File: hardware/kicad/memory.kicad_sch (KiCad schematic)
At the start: 21 parts, among them J201 microSD, U201 IS42S16400J-6TLI, U202 W25Q128JVSIQ

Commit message: Main PCB placement, layout rules, clock terminations, offline freerouting
- place_main_pcb.py: hand floorplan for the ICs plus a greedy placer
  (parts next to what they connect to, decoupling at their IC's power
  pins, clock series resistors at their MCU pins), inner planes
  In1 = GND / In2 = +3V3. CAP1188 moved top-middle between J302/J303.
- Net classes (Power, Rail3V3, Touch, Clock) set by gen_main_pcb.py and
  exported to the router; stm32-epaper.kicad_dru adds length/skew limits
  for the SDRAM/SDIO/QSPI buses, USB pair, crystals and touch lines,
  checked by KiCad DRC after routing.
- Schematic: 22/33R source series resistors R208-R210 on the SDRAM,
  microSD and QSPI clocks; check_schematic.py verifies they bridge the
  right nets.
- route_main_pcb.py: Specctra DSN/SES round trip for headless freerouting.
- .mcp.json: freerouting MCP server switched to the local jar (offline, no
  API key).
- docs/DS_stm32f469ae.pdf added; LSE margin checked (needs high-drive mode).
- Enclosure: fit-check print export (chin section + knob) and checklist.

Co-Authored-By: Claude Opus 5.5 <noreply@anthropic.com>
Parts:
- added R208, R210: 22R, Resistor_SMD:R_0402_1005Metric, symbol Device:R
- added R209: 33R, Resistor_SMD:R_0402_1005Metric, symbol Device:R
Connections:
- net FMC_SDCLK: now also R208.1; no longer U201.38 (CLK)
- net QUADSPI_CLK: now also R210.1; no longer U202.6 (CLK)
- net SDIO_CK: now also R209.1; no longer J201.5 (CLK)
- new net QSPI_FLASH_CLK: R210.2, U202.6 (CLK)
- new net SDCARD_CLK: J201.5 (CLK), R209.2
- new net SDRAM_CLK: R208.2, U201.38 (CLK)
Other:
- note added: "Clock series resistors (22-33R), placed right at the MCU pin: source termination for the SDRAM, microSD and QSPI clocks (point-to-point, up to 90 MHz)."

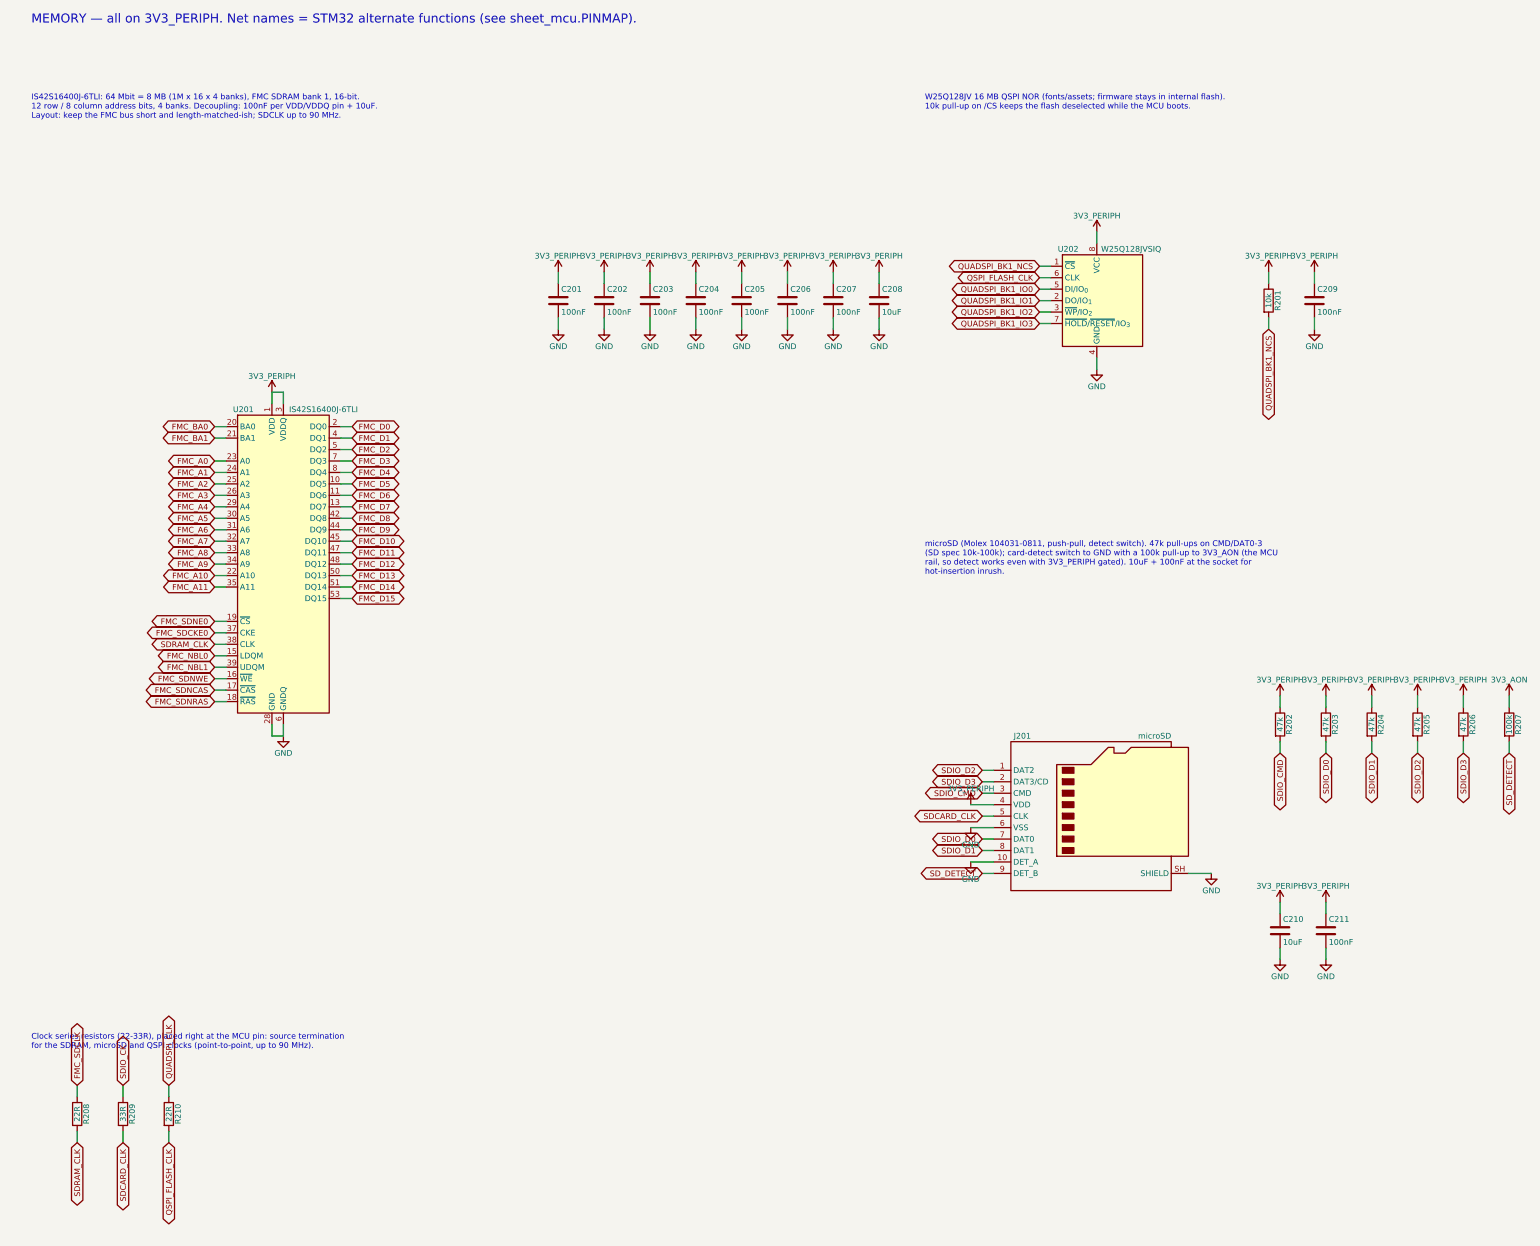
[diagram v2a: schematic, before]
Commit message: Schematic: Memory sheet redrawn with wired circuits
SDRAM VDD/VDDQ and QSPI VCC wired onto 3V3_PERIPH rails with their
decoupling banks; QSPI /CS pull-up tees off the line; microSD pull-ups
hang from a rail and drop onto each signal, VDD joins the rail with the
bulk/HF caps, VSS + DET_A share a GND column; the three clock series
resistors are drawn inline (device-side net names kept by label).
conn_by_name gains drawn= for pins the caller wires itself.
compare_netlists: electrically identical; board re-synced (0 unconnected,
0 parity issues).

Co-Authored-By: Claude Opus 5.5 <noreply@anthropic.com>
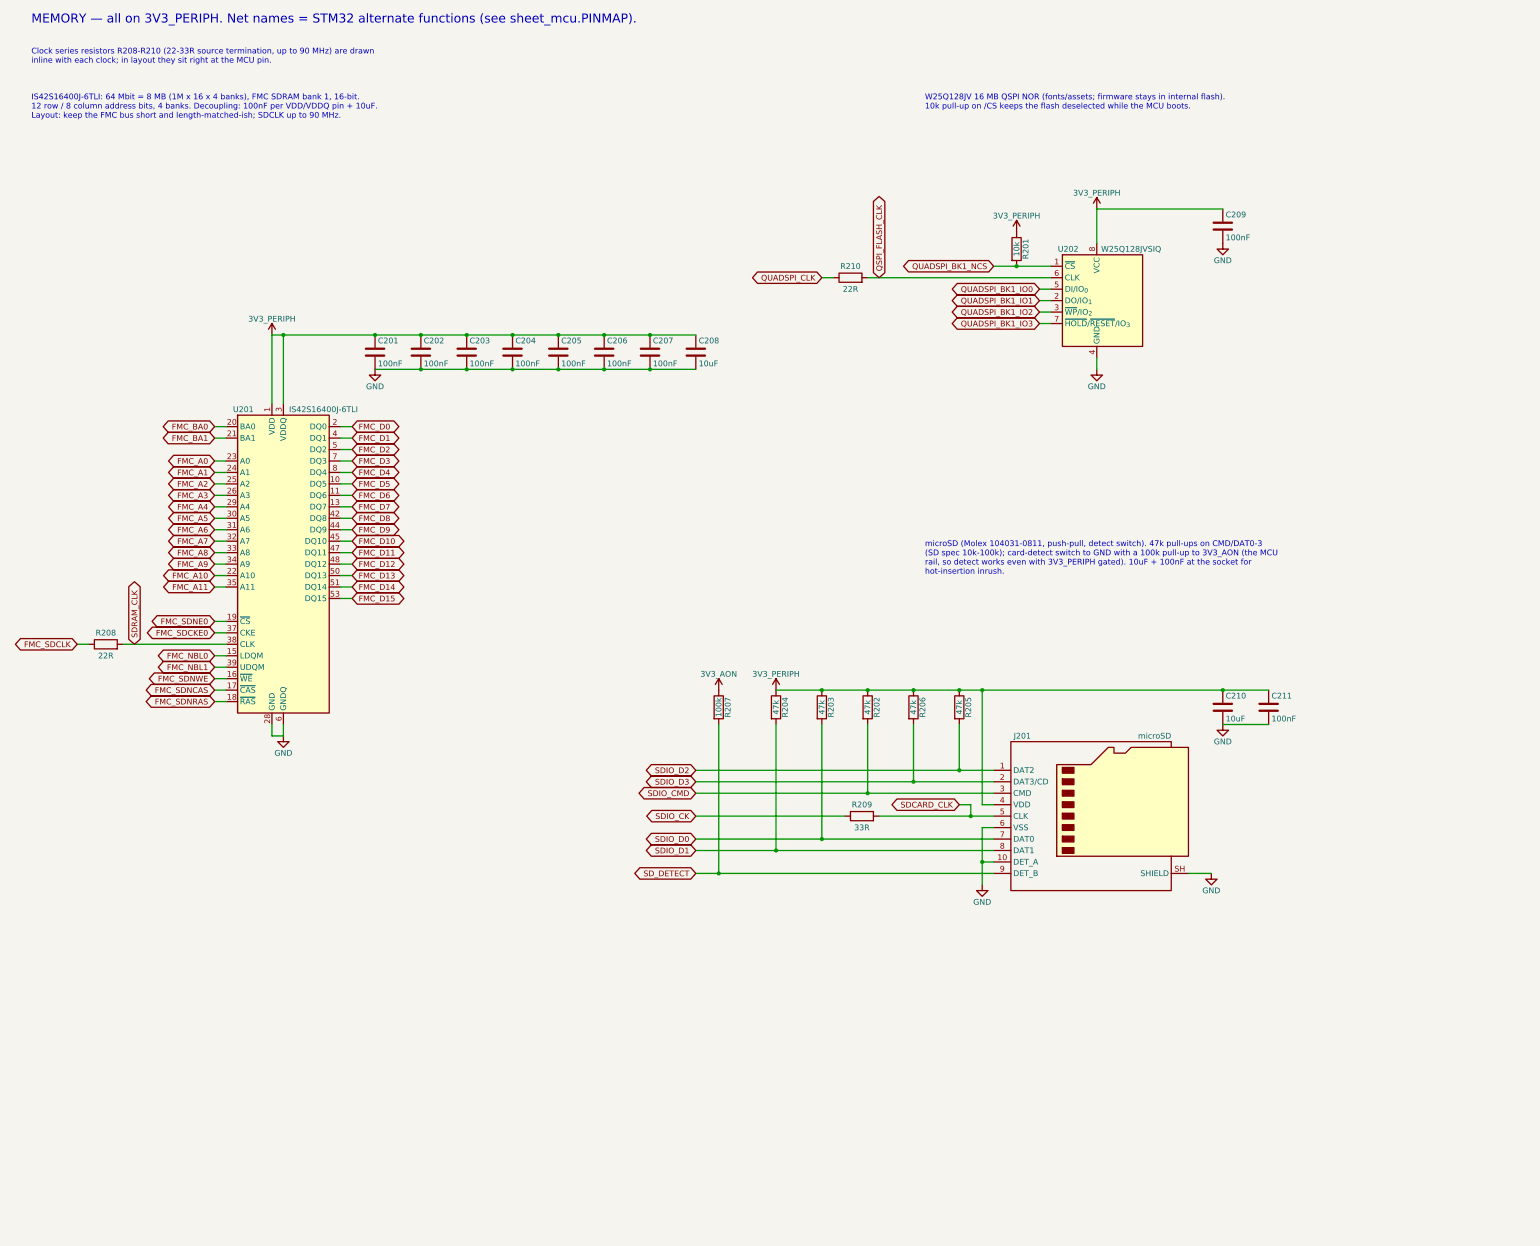
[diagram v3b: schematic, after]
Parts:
- removed C211: 100nF, Capacitor_SMD:C_0402_1005Metric, symbol Device:C
- removed U202: W25Q128JVSIQ, Package_SO:SOIC-8_5.3x5.3mm_P1.27mm, symbol Memory_Flash:W25Q128JVS
- added C208: 10uF, Capacitor_SMD:C_0805_2012Metric, symbol Device:C
- added R205: 47k, Resistor_SMD:R_0402_1005Metric, symbol Device:R
- C211: renamed from R205; value 47k -> 100nF; footprint Resistor_SMD:R_0402_1005Metric -> Capacitor_SMD:C_0402_1005Metric; symbol Device:R -> Device:C
- U202: renamed from C208; value 10uF -> W25Q128JVSIQ; footprint Capacitor_SMD:C_0805_2012Metric -> Package_SO:SOIC-8_5.3x5.3mm_P1.27mm; symbol Device:C -> Memory_Flash:W25Q128JVS; MPN (none) -> W25Q128JVSIQ
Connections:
- net 3V3_PERIPH: now also U202.8 (VCC), C208.1, R205.1; no longer U202.1
- net GND: now also C211.2, U202.4 (GND), C208.2; no longer U202.2
- net QSPI_FLASH_CLK: now also U202.6 (CLK)
- net QUADSPI_BK1_IO0: now also U202.5 (DI/IO_{0})
- net QUADSPI_BK1_IO1: now also U202.2 (DO/IO_{1})
- net QUADSPI_BK1_IO2: now also U202.3 (~{WP}/IO_{2})
- net QUADSPI_BK1_IO3: now also U202.7 (~{HOLD}/~{RESET}/IO_{3})
- net QUADSPI_BK1_NCS: now also U202.1 (~{CS})
- net SDIO_D2: now also R205.2; no longer C211.2
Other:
- note added: "Clock series resistors R208-R210 (22-33R source termination, up to 90 MHz) are drawn inline with each clock; in layout they sit right at the MCU pin."
- note removed: "Clock series resistors (22-33R), placed right at the MCU pin: source termination for the SDRAM, microSD and QSPI clocks (point-to-point, up to 90 MHz)."
